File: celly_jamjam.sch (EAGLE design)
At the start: 58 parts, among them T1 2N3904, U1 OSCILLATOR5X3

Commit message: finished schematic, now onto board. jeeez
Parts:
- removed ICL7660: (no value), ic-package:DIL8
- added FERRITEBEADLEAD: type43, inductors:BLM15HB121SN1
- added IC1: M3500-1324S/T, burr-brown:OPA642N
- added MICROSTRIPLINE, MICROSTRIPLN2: 50 Ohm, inductors:BLM15HB121SN1
- added RFOUTPUTANTENNA: 80mW, SparkFun-RF:ANTENNASMD1
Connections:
- new net N$33: C9.1, IC1.+IN
- new net N$34: MICROSTRIPLN2.2, RFOUTPUTANTENNA.SIGNAL
- new net N$35: C9.2, MICROSTRIPLINE.2
- new net N$36: FERRITEBEADLEAD.2, R16.1
- new net N$37: MICROSTRIPLN2.1
- net GND: now also IC1.V+, IC1.V-, RFOUTPUTANTENNA.GND, VOLTAGEINVERT.GND; no longer ICL7660.3
- net N$17: now also IC1.OUT
- net N$2: now also FERRITEBEADLEAD.1; no longer R16.1
- net N$28: now also MICROSTRIPLINE.1
- net N$4: now also C17.+, VOLTAGEINVERT.CAP+; no longer C17.-, ICL7660.4
- net N$5: now also C17.-, VOLTAGEINVERT.CAP-; no longer C17.+, ICL7660.2
- net N$7: now also VOLTAGEINVERT.VOUT; no longer ICL7660.5
- net VCC: now also VOLTAGEINVERT.NC, VOLTAGEINVERT.V+; no longer ICL7660.1, ICL7660.8
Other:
- moved on the sheet: C10, C16, C17, C2, C7, C8, C9, L2, R16, VOLTAGEINVERT

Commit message: design is better
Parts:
- removed MICROSTRIPLN2: 50 Ohm, inductors:BLM15HB121SN1
- removed TRANSISTOR: MPF102, transistor-small-signal:MMBFJ3
- added MICROSTRIPLINE1: 50 Ohm, inductors:BLM15HB121SN1
- added Q1: mpf102, transistor-fet:BF245
- C10, C9: value (none) -> 68pF
- C12: value (none) -> 0.1uF
- IC1: value M3500-1324S/T -> AG603-86
- U1: value OSCILLATOR5X3 -> M3500
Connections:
- removed net N$34 (its old number): MICROSTRIPLN2.2, RFOUTPUTANTENNA.SIGNAL
- removed net N$37: MICROSTRIPLN2.1
- new net N$17: C10.1, MICROSTRIPLINE1.1
- new net N$40: MICROSTRIPLINE1.2, RFOUTPUTANTENNA.SIGNAL
- net N$24: now also Q1.G; no longer TRANSISTOR.G
- net N$27: now also Q1.D; no longer TRANSISTOR.D
- net N$30: now also Q1.S; no longer TRANSISTOR.S
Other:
- moved on the sheet: C1, C10, C18, C19, C2, C7, C8, D1, FERRITEBEADLEAD, L2, R13, R14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

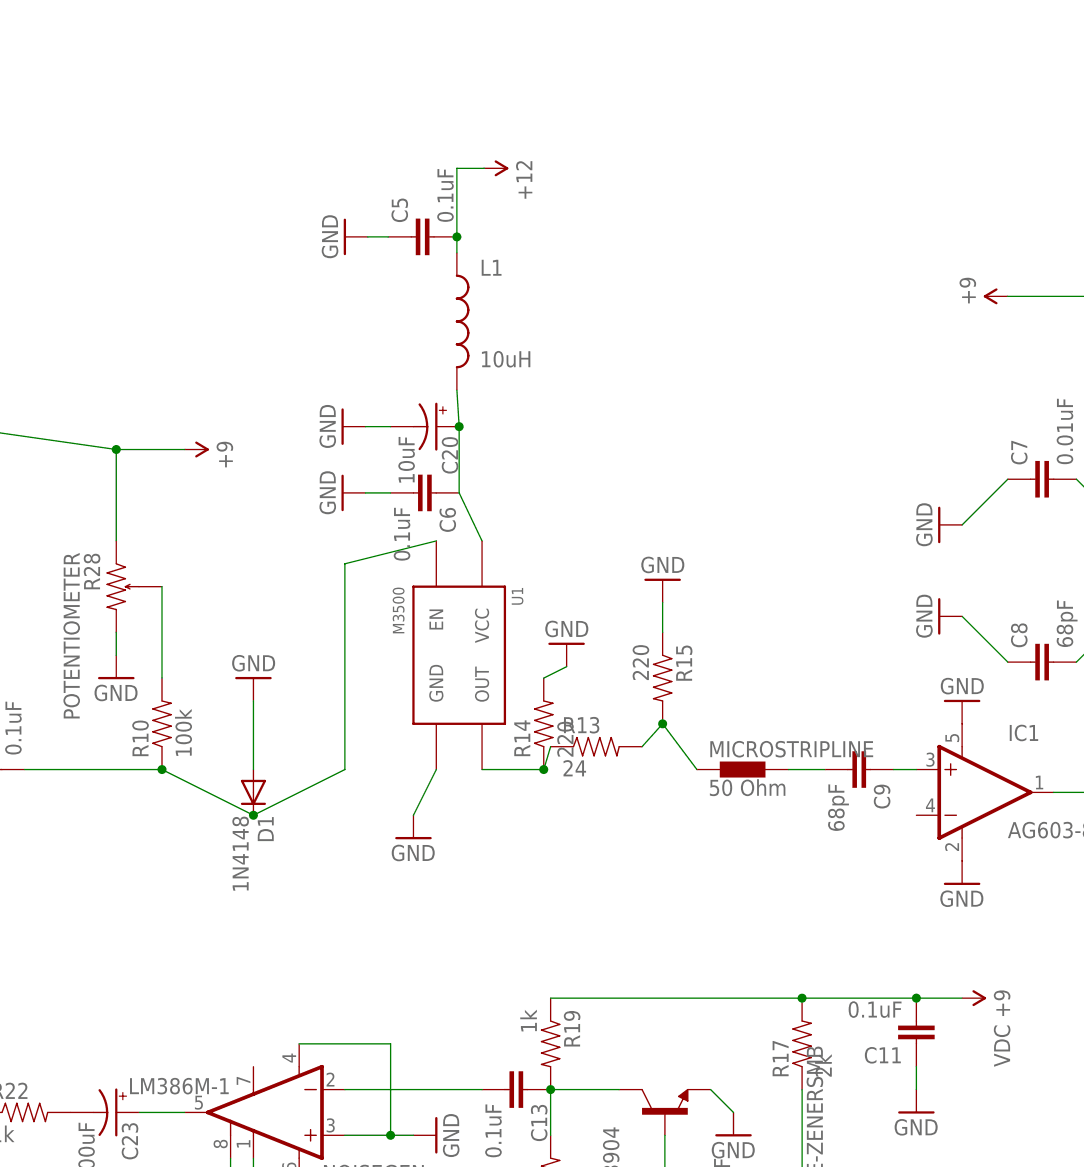
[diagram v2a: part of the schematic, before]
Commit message: added correct VCO
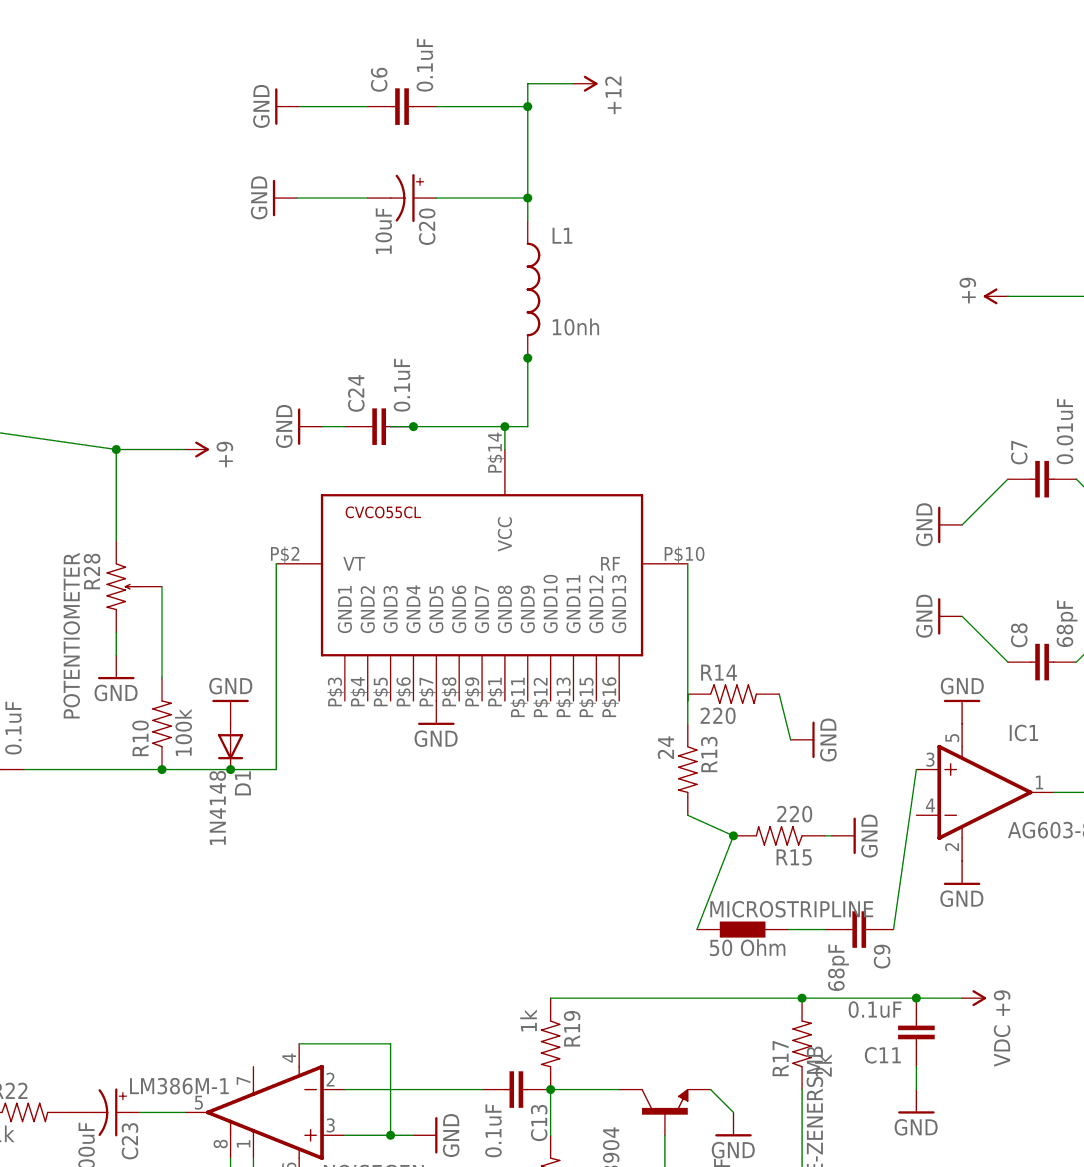
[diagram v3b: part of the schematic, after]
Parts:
- removed C5: 0.1uF, SparkFun-Passives:CAP0603-CAP
- removed U1: M3500, SparkFun-FreqCtrl:OSCILLATOR5X3
- added C24: 0.1uF, SparkFun-Passives:CAP0603-CAP
- added U$1: CVCO55CL, crystec_vco:CVCO55CL
- L1: value 10uH -> 10nh
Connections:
- new net N$37: C24.2, L1.2, U$1.VCC
- net GND: now also C24.1, C6.1, U$1.GND5; no longer C5.1, C6.2, U1.GND
- net N$29: no longer U1.OUT
- net N$3: now also U$1.RF; no longer C20.+, C6.1, L1.2, U1.VCC
- net N$32: now also U$1.VT; no longer U1.EN
- net VCC: now also C20.+, C6.2; no longer C5.2
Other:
- moved on the sheet: C20, C6, C9, D1, L1, MICROSTRIPLINE, R13, R14, R15

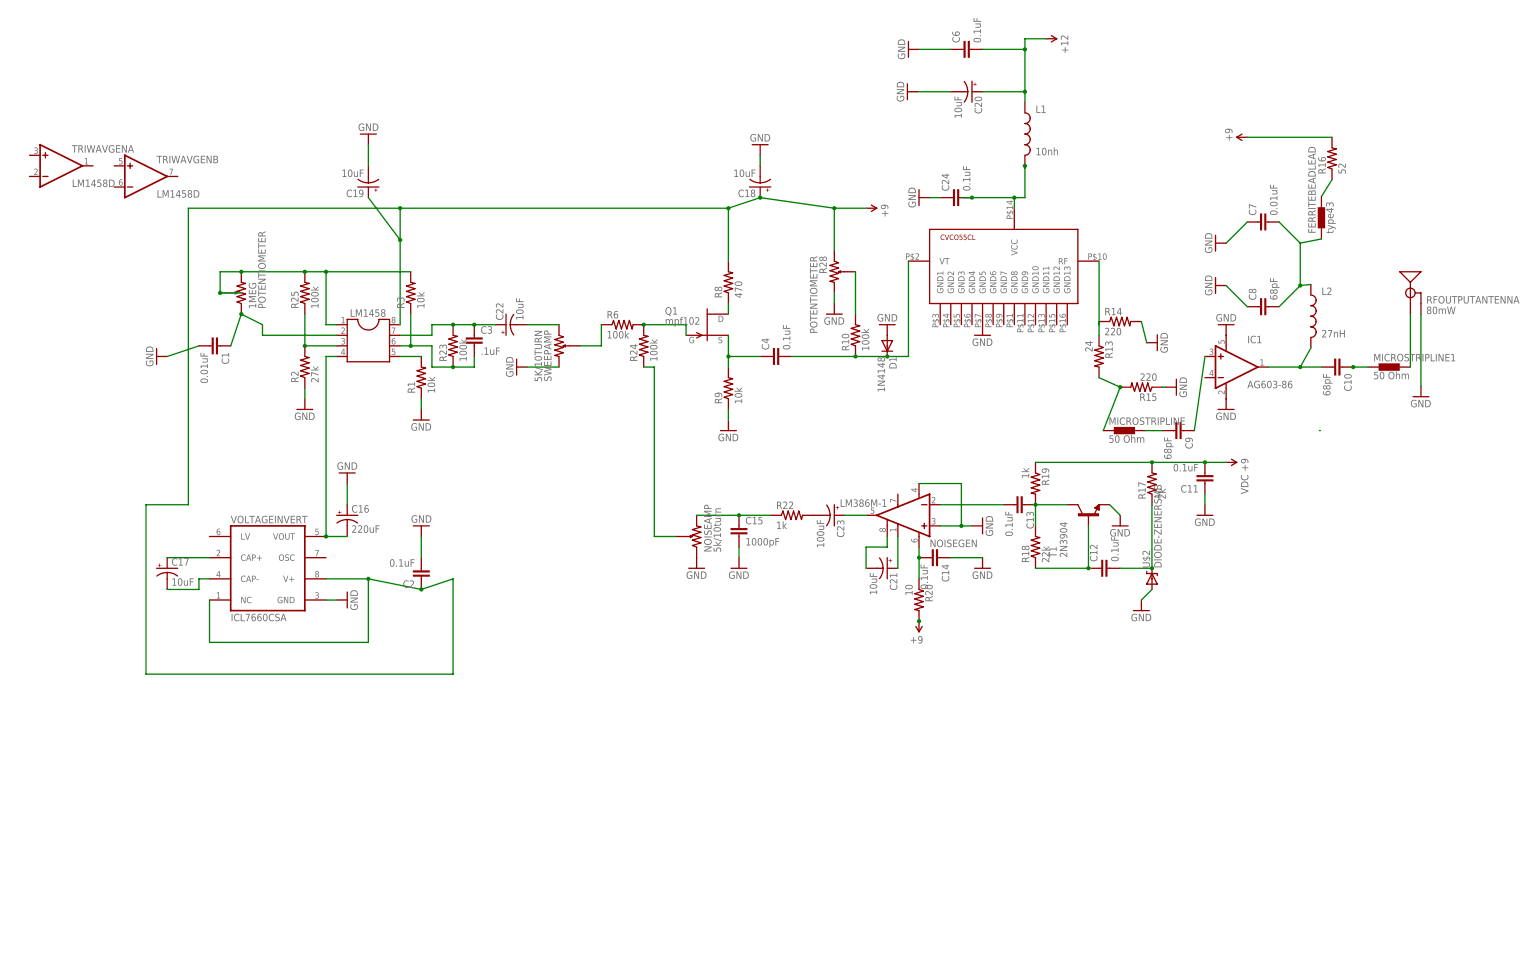
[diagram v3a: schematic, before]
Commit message: changed everything to SMD. much work to be done
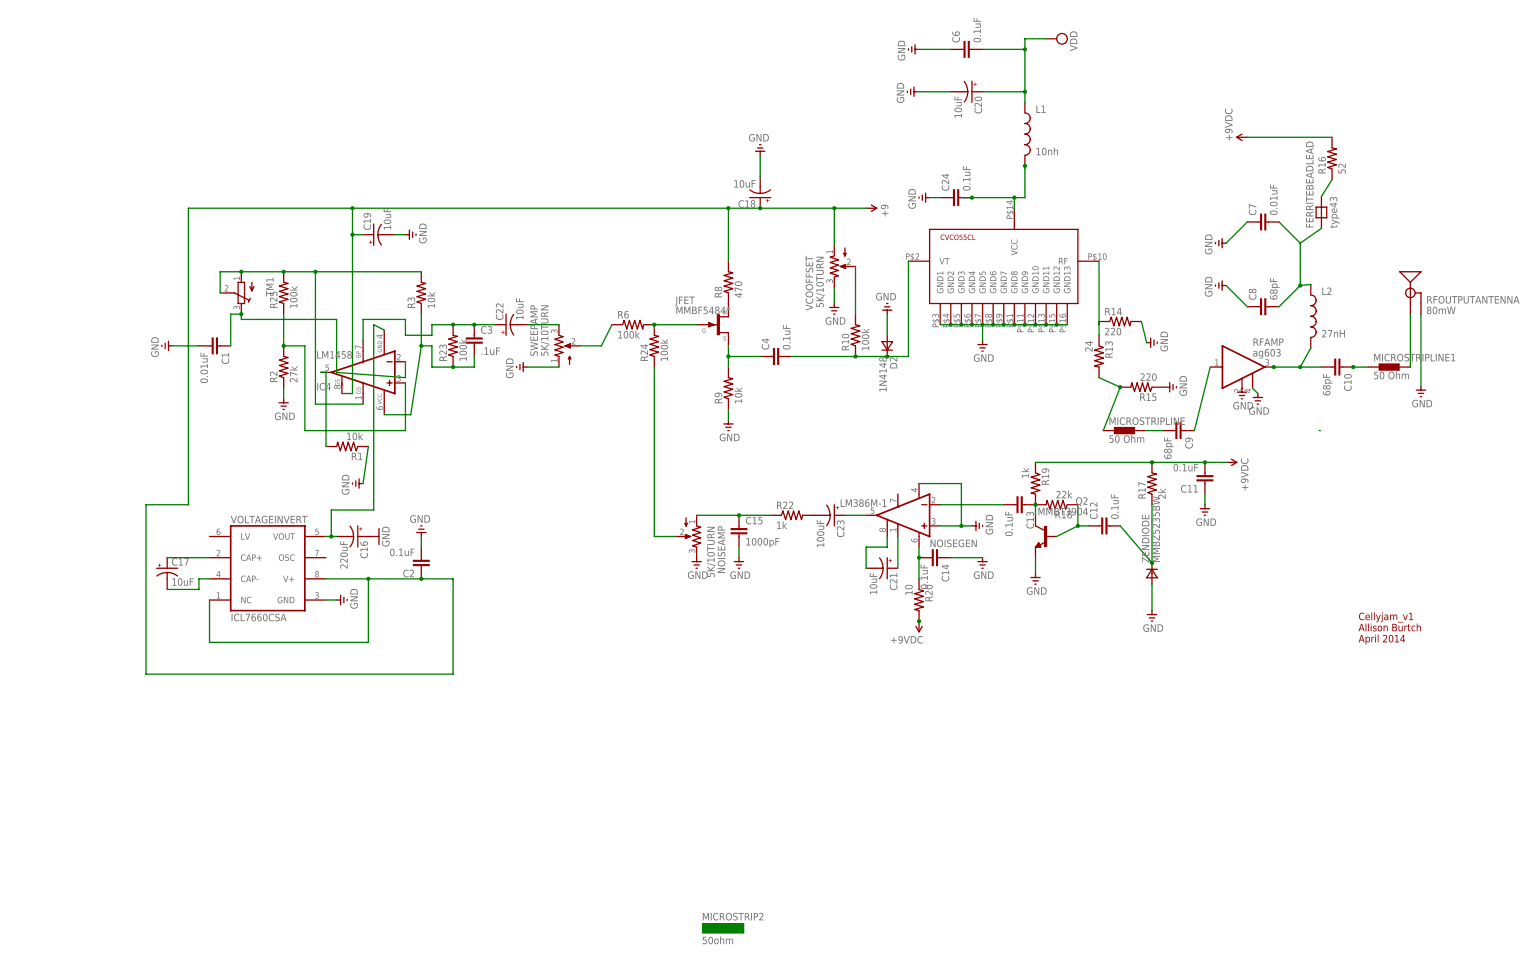
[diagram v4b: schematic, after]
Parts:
- removed 1MEG, R28: POTENTIOMETER, SparkFun-Passives:POTENTIOMETER
- removed D1: 1N4148, SparkFun-DiscreteSemi:DIODE1N4148
- removed IC1: AG603-86, burr-brown:OPA642N
- removed LM1458: (no value), ic-package:DIL8
- removed Q1: mpf102, transistor-fet:BF245
- removed T1: 2N3904, transistor:2N3904
- removed TRIWAVGEN: LM1458D, linear:LM1458D
- removed U$2: DIODE-ZENERSMB, SparkFun-DiscreteSemi:DIODE-ZENERSMB
- added D2: 1N4148, zetex:DSOD323
- added IC4: LM1458, linear:LM386M
- added JFET: MMBF5484*, transistor-fet:MMBF5484
- added Q2: MMBT3904, transistor-npn:MMBT3904
- added RFAMP: ag603, mini-circuits:LEE-39+
- added TM1: (no value), adafruit:TRIMPOTTC33X
- added VCOOFFSET: 5K/10TURN, pot:P160KN
- added ZENDIODE: MMBZ5235BW, zetex:DSOD323
- C16, C23: device SparkFun-Capacitors:CAP_POL1206 -> SparkFun-Capacitors:CAP_POLD
- C17, C18, C19, C20, C21, C22: device SparkFun-Capacitors:CAP_POL1206 -> SparkFun-Capacitors:CAP_POLC
- FERRITEBEADLEAD: device inductors:BLM15HB121SN1 -> inductor-jwmiller:FB-226
- NOISEAMP: value 5k/10turn -> 5K/10TURN; device SparkFun-Passives:POTENTIOMETER -> pot:P160KN
- SWEEPAMP: device SparkFun-Passives:POTENTIOMETER -> pot:P160KN
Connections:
- removed net N$1: LM1458.5, R1.2
- removed net N$13: C22.+, C3.1, LM1458.7, R23.2
- removed net N$9: LM1458.3, R2.2, R25.1
- new net N$47: JFET.G, R24.2, R6.2
- new net N$48: IC4.OUT, R1.2
- new net N$49: IC4.+IN, R2.2, R25.1
- new net VDD: C20.+, C6.2, L1.1
- net GND: now also D2.A, NOISEAMP.3, Q2.E, RFAMP.GND@1, RFAMP.GND@2, SWEEPAMP.1, U$1.GND1, U$1.GND10, U$1.GND11, U$1.GND12, U$1.GND13, U$1.GND2, U$1.GND3, U$1.GND4, U$1.GND6, U$1.GND7, U$1.GND8, U$1.GND9, VCOOFFSET.3, ZENDIODE.A; no longer D1.A, IC1.V+, IC1.V-, NOISEAMP.1, R28.2, SWEEPAMP.2, T1.E, U$2.A
- net N$10: now also IC4.-IN, TM1.E; no longer 1MEG.1, LM1458.2
- net N$11: now also SWEEPAMP.2; no longer SWEEPAMP.P$1
- net N$12: now also SWEEPAMP.3; no longer SWEEPAMP.1
- net N$14: now also IC4.VS; no longer LM1458.6
- net N$16: now also Q2.B; no longer T1.B
- net N$19: now also Q2.C; no longer T1.C
- net N$20: now also ZENDIODE.C; no longer U$2.C
- net N$23: now also NOISEAMP.1; no longer NOISEAMP.2
- net N$24: now also C22.+, C3.1, IC4.BS2, R23.2; no longer Q1.G, R24.2, R6.2
- net N$25: now also NOISEAMP.2; no longer NOISEAMP.P$1
- net N$27: now also JFET.D; no longer Q1.D
- net N$30: now also JFET.S; no longer Q1.S
- net N$31: now also VCOOFFSET.2; no longer R28.P$1
- net N$32: now also D2.C; no longer D1.C
- net N$33: now also RFAMP.IN; no longer IC1.+IN
- net N$34: now also RFAMP.OUT; no longer IC1.OUT
- net N$7: now also IC4.GND; no longer LM1458.4
- net N$8: now also IC4.GAIN@1, TM1.A, TM1.S; no longer 1MEG.2, 1MEG.P$1, LM1458.1
- net VCC: now also IC4.GAIN@8, VCOOFFSET.1; no longer C20.+, C6.2, L1.1, LM1458.8, R28.1
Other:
- note added: "Cellyjam_v1 Allison Burtch April 2014"
- moved on the sheet: C12, C16, C18, C19, C2, R1, R18, R2, R24, R25, R3, R6
